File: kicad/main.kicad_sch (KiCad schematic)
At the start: 25 parts, among them J1 Barrel_Jack, Q1 Q_NJFET_DGS, Q10 Q_NJFET_GSD, Q11 Q_NJFET_SDG, Q12 Q_NJFET_SGD, Q2 Q_NJFET_DSG, Q3 Q_NJFET_GDS, Q4 Q_NJFET_GSD, Q5 Q_NJFET_SDG, Q6 Q_NJFET_SGD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

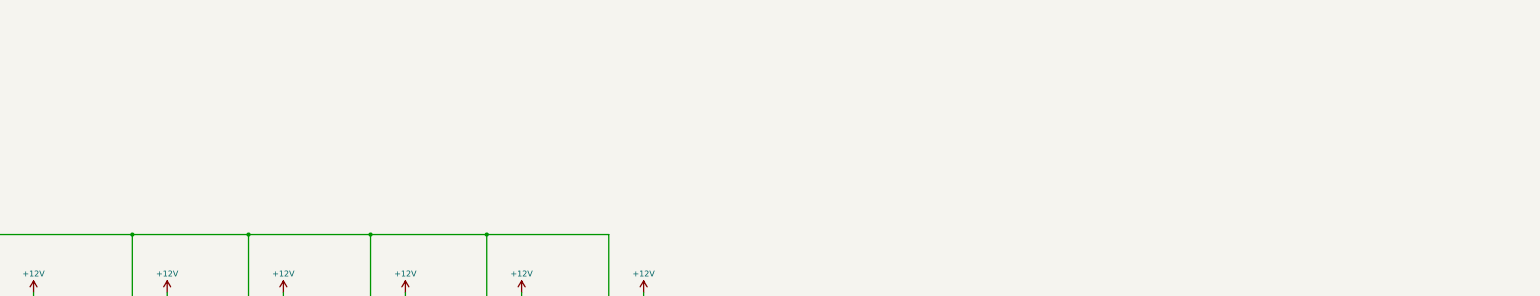
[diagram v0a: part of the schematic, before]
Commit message: wider pinout
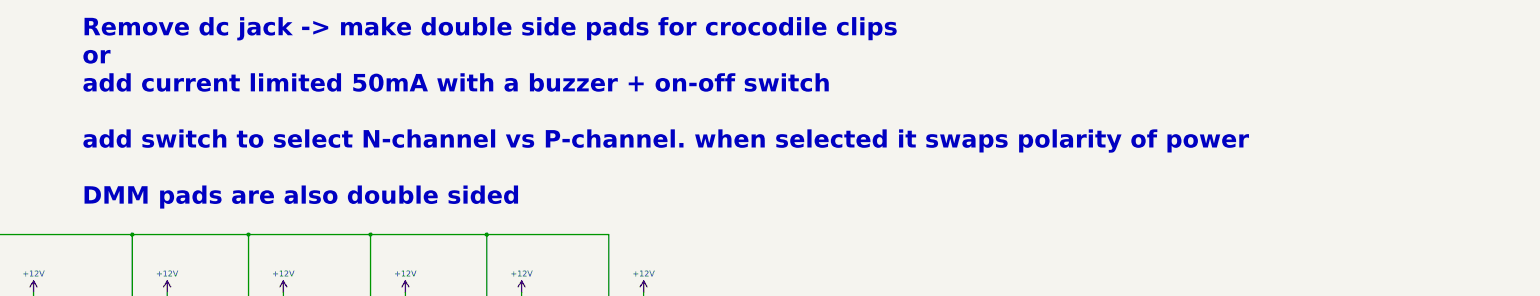
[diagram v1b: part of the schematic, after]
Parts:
- Q1, Q2, Q3, Q4, Q5, Q6: footprint Package_TO_SOT_THT:TO-92_Inline -> Package_TO_SOT_THT:TO-92_Inline_Wide
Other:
- note added: "Remove dc jack -> make double side pads for crocodile clips or add current limited 50mA with a buzzer + on-off switch add switch to select N-channel vs P-channel. when selected it swaps polarity of power DMM pads are also double sided"
